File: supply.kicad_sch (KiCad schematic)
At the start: 1 part

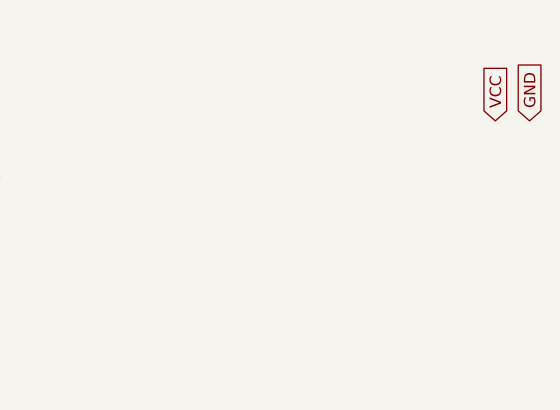
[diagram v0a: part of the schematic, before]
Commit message: now using correct VCC and GND symbols
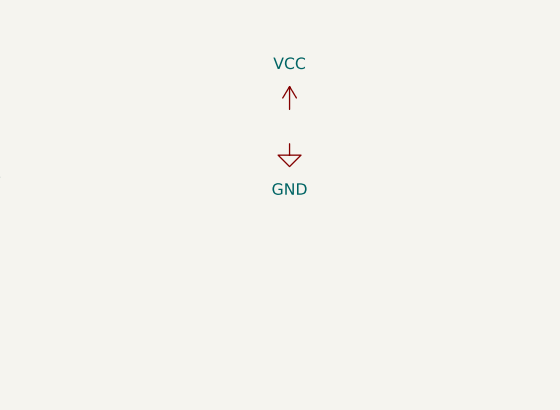
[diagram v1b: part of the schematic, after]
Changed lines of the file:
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@@
 (kicad_sch (version 20211123) (generator eeschema)
   (paper "A4")
-  (global_label "VCC" (shape input) (at 144.78 36.83 90) (fields_autoplaced)
-    (effects (font (size 1.27 1.27)) (justify left))
-    (property "Intersheet References" "${INTERSHEET_REFS}" (id 0) (at 144.7006 30.7883 90)
-      (effects (font (size 1.27 1.27)) (justify left) hide)
+  (symbol (lib_id "power:GND") (at 121.92 39.37 0) (unit 1)
+    (in_bom yes) (on_board yes) (fields_autoplaced)
+    (property "Reference" "#PWR?" (id 0) (at 121.92 45.72 0)
+      (effects (font (size 1.27 1.27)) hide)
     )
-  )
-  (global_label "GND" (shape input) (at 148.59 36.83 90) (fields_autoplaced)
-    (effects (font (size 1.27 1.27)) (justify left))
-    (property "Intersheet References" "${INTERSHEET_REFS}" (id 0) (at 148.5106 30.5464 90)
-      (effects (font (size 1.27 1.27)) (justify left) hide)
+    (property "Value" "GND" (id 1) (at 121.92 44.45 0))
+    (property "Footprint" "" (id 2) (at 121.92 39.37 0)
+      (effects (font (size 1.27 1.27)) hide)
     )
+    (property "Datasheet" "" (id 3) (at 121.92 39.37 0)
+      (effects (font (size 1.27 1.27)) hide)
+    )
+    (pin "1")
   )
   (symbol (lib_id "supply:ISL9307IRTAANFZ-T7A") (at 38.1 45.72 0) (unit 1)
@@
     (pin "9")
   )
+  (symbol (lib_id "power:VCC") (at 121.92 35.56 0) (unit 1)
+    (in_bom yes) (on_board yes) (fields_autoplaced)
+    (property "Reference" "#PWR?" (id 0) (at 121.92 39.37 0)
+      (effects (font (size 1.27 1.27)) hide)
+    )
+    (property "Value" "VCC" (id 1) (at 121.92 30.48 0))
+    (property "Footprint" "" (id 2) (at 121.92 35.56 0)
+      (effects (font (size 1.27 1.27)) hide)
+    )
+    (property "Datasheet" "" (id 3) (at 121.92 35.56 0)
+      (effects (font (size 1.27 1.27)) hide)
+    )
+    (pin "1")
+  )
 )

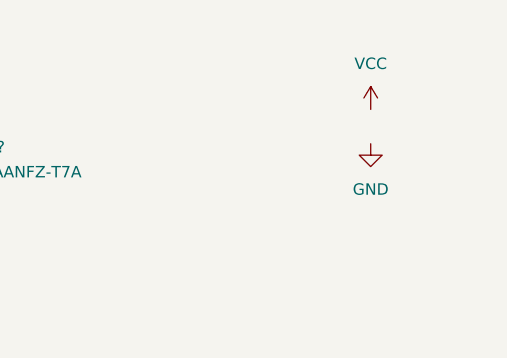
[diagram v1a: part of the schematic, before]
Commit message: added esp32 schematic && updated supply symbols
Signed-off-by: Tobias Gent <gent.tobias@gmail.com>
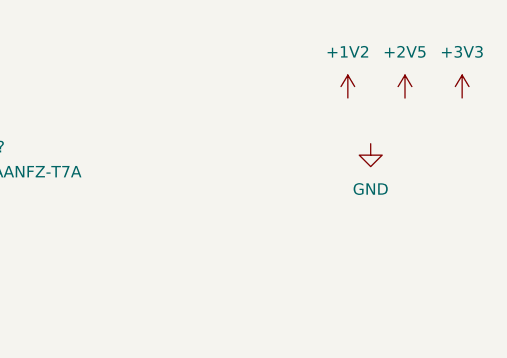
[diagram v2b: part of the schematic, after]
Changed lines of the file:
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@@
     (pin "9")
   )
-  (symbol (lib_id "power:VCC") (at 121.92 35.56 0) (unit 1)
+  (symbol (lib_id "power:+2V5") (at 125.73 34.29 0) (unit 1)
     (in_bom yes) (on_board yes) (fields_autoplaced)
-    (property "Reference" "#PWR?" (id 0) (at 121.92 39.37 0)
+    (property "Reference" "#PWR?" (id 0) (at 125.73 38.1 0)
       (effects (font (size 1.27 1.27)) hide)
     )
-    (property "Value" "VCC" (id 1) (at 121.92 30.48 0))
-    (property "Footprint" "" (id 2) (at 121.92 35.56 0)
+    (property "Value" "+2V5" (id 1) (at 125.73 29.21 0))
+    (property "Footprint" "" (id 2) (at 125.73 34.29 0)
       (effects (font (size 1.27 1.27)) hide)
     )
-    (property "Datasheet" "" (id 3) (at 121.92 35.56 0)
+    (property "Datasheet" "" (id 3) (at 125.73 34.29 0)
       (effects (font (size 1.27 1.27)) hide)
     )
+    (pin "1")
+  )
+  (symbol (lib_id "power:+1V2") (at 119.38 34.29 0) (unit 1)
+    (in_bom yes) (on_board yes) (fields_autoplaced)
+    (property "Reference" "#PWR?" (id 0) (at 119.38 38.1 0)
+      (effects (font (size 1.27 1.27)) hide)
+    )
+    (property "Value" "+1V2" (id 1) (at 119.38 29.21 0))
+    (property "Footprint" "" (id 2) (at 119.38 34.29 0)
+      (effects (font (size 1.27 1.27)) hide)
+    )
+    (property "Datasheet" "" (id 3) (at 119.38 34.29 0)
+      (effects (font (size 1.27 1.27)) hide)
+    )
+    (pin "1")
+  )
+  (symbol (lib_id "power:+3V3") (at 132.08 34.29 0) (unit 1)
+    (in_bom yes) (on_board yes) (fields_autoplaced)
+    (property "Reference" "#PWR?" (id 0) (at 132.08 38.1 0)
+      (effects (font (size 1.27 1.27)) hide)
+    )
+    (property "Value" "+3V3" (id 1) (at 132.08 29.21 0))
+    (property "Footprint" "" (id 2) (at 132.08 34.29 0)
+      (effects (font (size 1.27 1.27)) hide)
+    )
+    (property "Datasheet" "" (id 3) (at 132.08 34.29 0)
+      (effects (font (size 1.27 1.27)) hide)
+    )

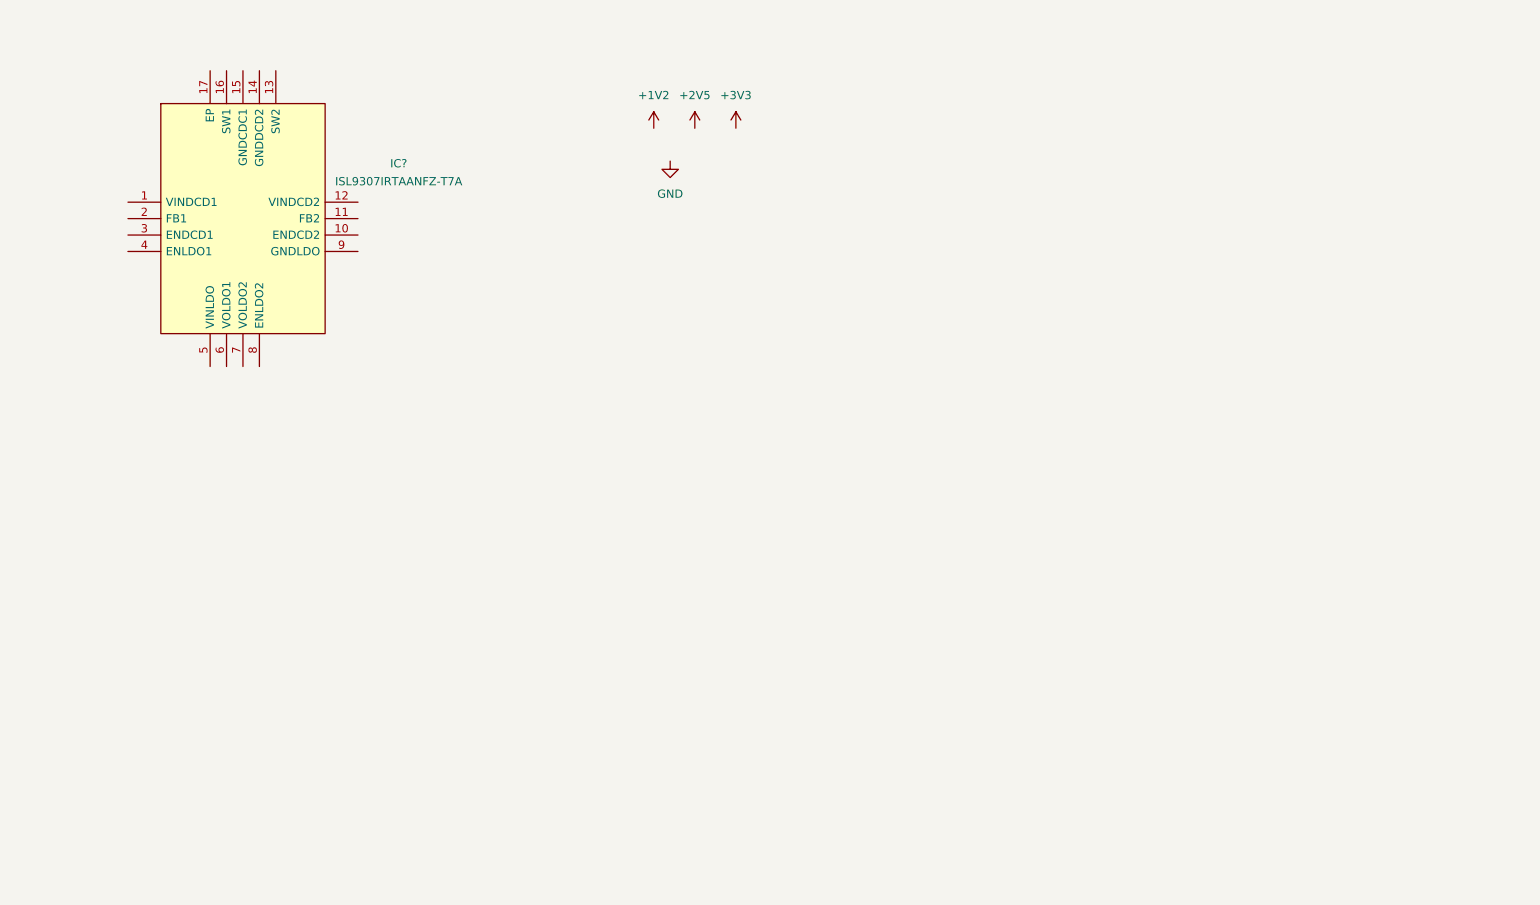
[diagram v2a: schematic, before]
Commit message: Added Supply
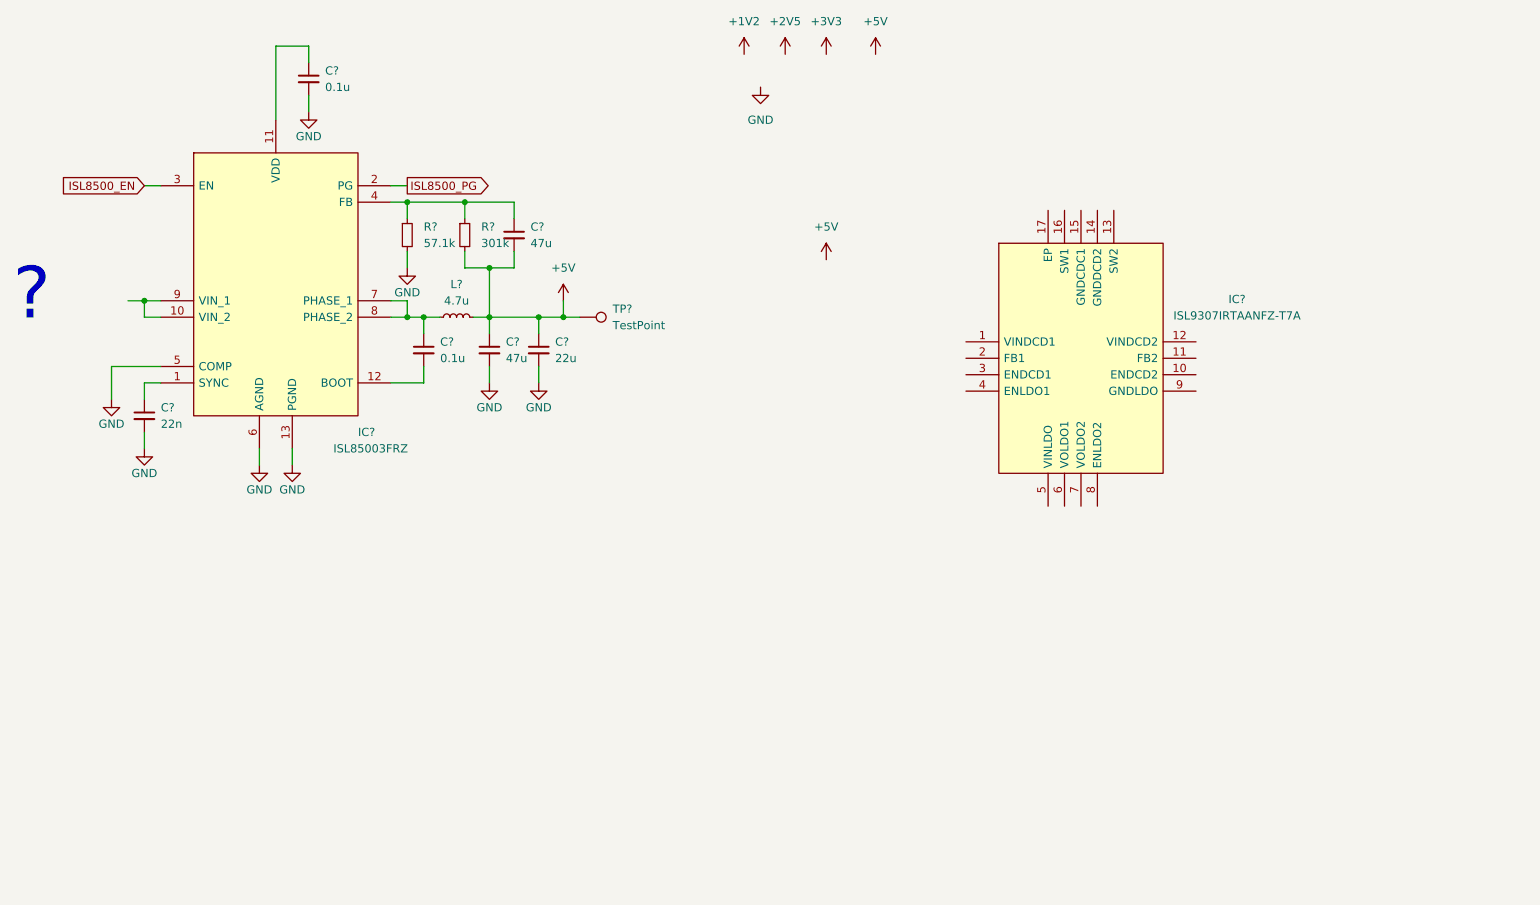
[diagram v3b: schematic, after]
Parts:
- added C?: 22u, symbol Device:C_Small
- added C? (x2): 47u, symbol Device:C_Small
- added C? (x2): 0.1u, symbol Device:C_Small
- added C?: 22n, symbol Device:C_Small
- added IC?: ISL85003FRZ, SON50P300X400X90-13N, symbol supply:ISL85003FRZ
- added L?: 4.7u, symbol Device:L_Small
- added R?: 301k, symbol Device:R_Small
- added R?: 57.1k, symbol Device:R_Small
- added TP?: TestPoint, symbol Connector:TestPoint
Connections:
- net GND: now also C?.2, C?.2, C?.2, C?.2, IC?.13 (PGND), IC?.5 (COMP), IC?.6 (AGND), R?.2
- new net: C?.1, IC?.4 (FB), R?.1, R?.1
- new net: C?.1, IC?.1 (SYNC)
- new net: IC?.10 (VIN_2), IC?.9 (VIN_1)
- new net: C?.1, IC?.11 (VDD)
- new net: C?.2, IC?.12 (BOOT)
- new net: C?.1, IC?.7 (PHASE_1), IC?.8 (PHASE_2), L?.1
- new net +5V: C?.1, C?.1, C?.2, L?.2, R?.2, TP?.1
- new net ISL8500_EN: IC?.3 (EN)
- new net ISL8500_PG: IC?.2 (PG)
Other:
- note added: "?"
- moved on the sheet: IC?

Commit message: modified supply symbols + added layout
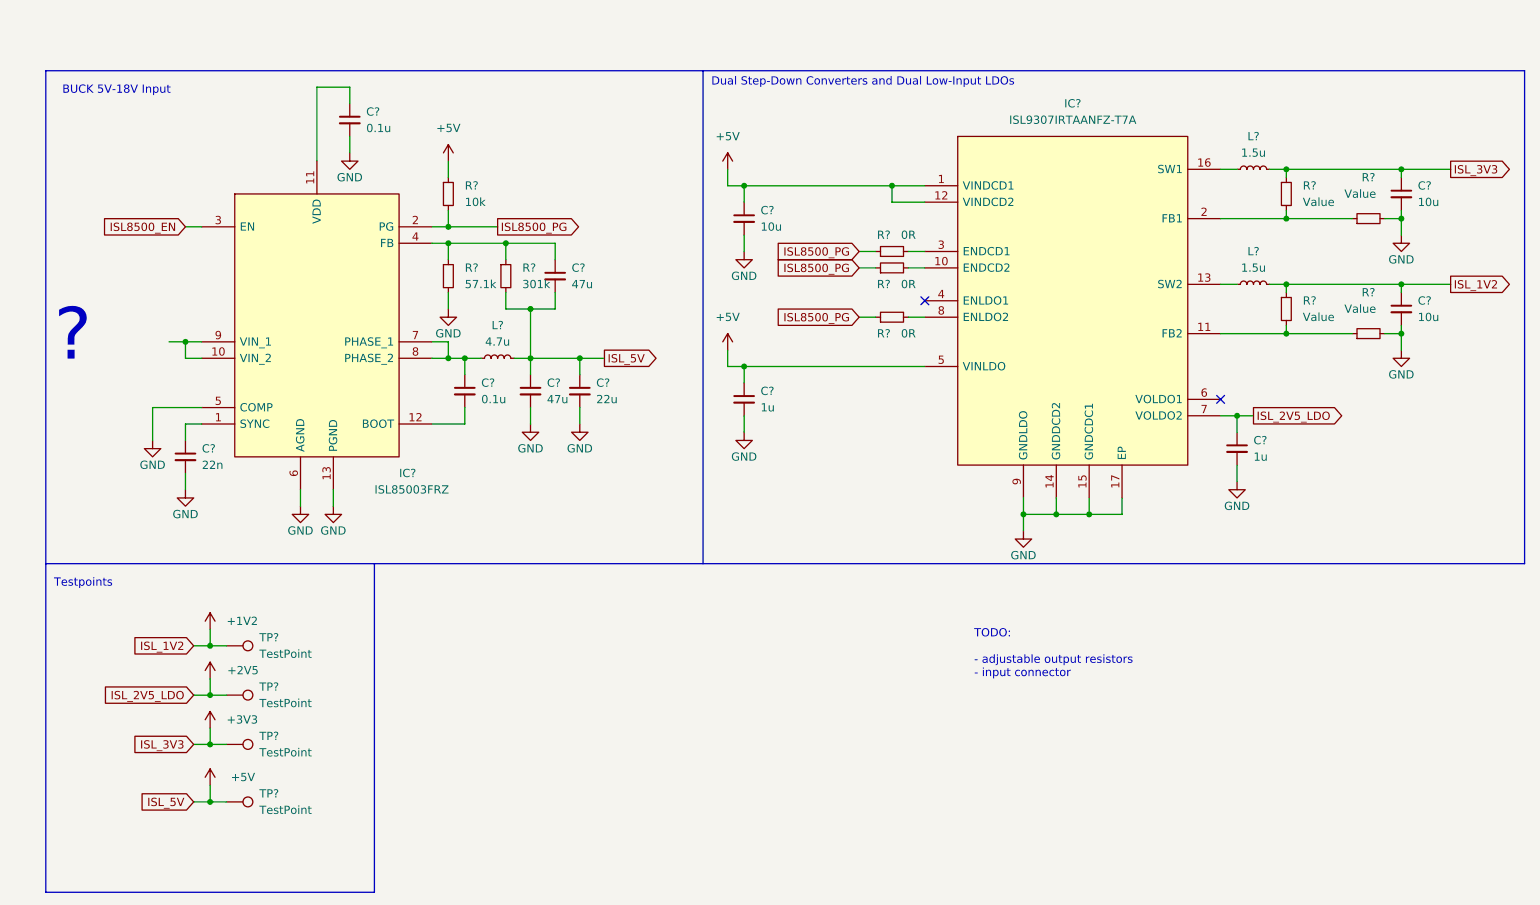
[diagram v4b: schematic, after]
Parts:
- removed TP?: TestPoint, symbol Connector:TestPoint
- added C? (x3): 10u, symbol Device:C_Small
- added C? (x2): 1u, symbol Device:C_Small
- added L? (x2): 1.5u, symbol Device:L_Small
- added R? (x4): Value, symbol Device:R_Small
- added R? (x3): 0R, symbol Device:R_Small
- added R?: 10k, symbol Device:R_Small
- added TP? (x4): TestPoint, symbol Connector:TestPoint
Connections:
- net +1V2: now also C?.1, L?.2, R?.1, TP?.1
- net +2V5: now also IC?.7 (VOLDO2), C?.1, TP?.1
- net +3V3: now also C?.1, L?.2, R?.1, TP?.1
- net +5V: now also IC?.1 (VINDCD1), IC?.12 (VINDCD2), IC?.5 (VINLDO), C?.1, C?.1, R?.1, TP?.1
- net GND: now also IC?.14 (GNDDCD2), IC?.15 (GNDCDC1), IC?.17 (EP), IC?.9 (GNDLDO), C?.2, C?.2, C?.2, C?.2, C?.2, R?.2, R?.2
- net ISL8500_PG: now also R?.1, R?.1, R?.1, R?.2
- net at IC?.10 (ENDCD2): now also R?.2
- net at IC?.11 (FB2): now also R?.1, R?.2
- net at IC?.13 (SW2): now also L?.1
- net at IC?.16 (SW1): now also L?.1
- net at IC?.2 (FB1): now also R?.1, R?.2
- net at IC?.3 (ENDCD1): now also R?.2
- net at IC?.8 (ENLDO2): now also R?.2
- no-connect marks 0 -> 2
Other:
- note added: "BUCK 5V-18V Input"
- note added: "Dual Step-Down Converters and Dual Low-Input LDOs"
- note added: "TODO: - adjustable output resistors - input connector"
- note added: "Testpoints"
- moved on the sheet: C?, IC?, L?, R?

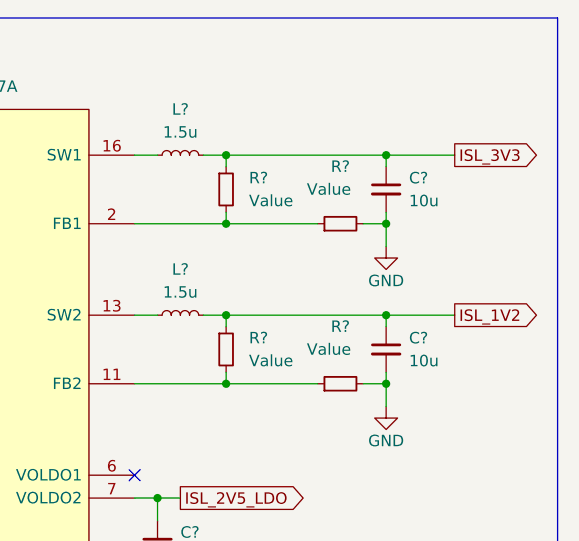
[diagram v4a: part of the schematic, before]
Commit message: supply: changed voltage divider values on ISL9307
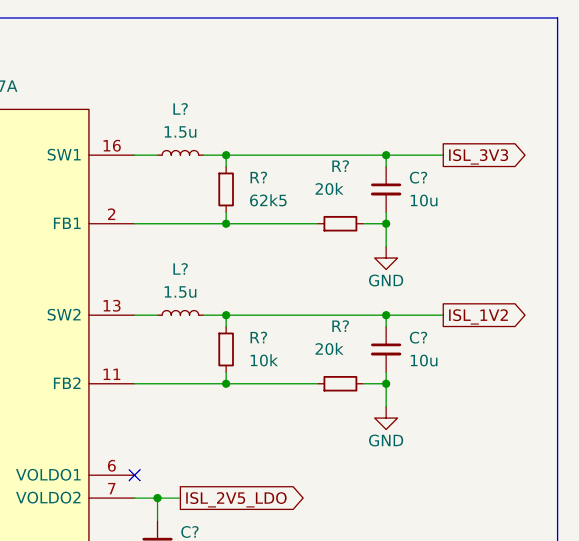
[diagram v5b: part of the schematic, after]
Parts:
- R?: value Value -> 62k5
- R?: value Value -> 10k
- R? (x2): value Value -> 20k
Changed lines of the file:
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@@
     (stroke (width 0) (type default) (color 0 0 0 0))
   )
-  (wire (pts (xy 234.95 58.42) (xy 242.57 58.42))
+  (wire (pts (xy 234.95 58.42) (xy 241.3 58.42))
     (stroke (width 0) (type default) (color 0 0 0 0))
   )
@@
     (stroke (width 0) (type default) (color 0 0 0 0))
   )
-  (wire (pts (xy 234.95 40.64) (xy 242.57 40.64))
+  (wire (pts (xy 234.95 40.64) (xy 241.3 40.64))
     (stroke (width 0) (type default) (color 0 0 0 0))
   )
@@
     )
   )
-  (global_label "ISL_1V2" (shape output) (at 242.57 58.42 0) (fields_autoplaced)
+  (global_label "ISL_1V2" (shape output) (at 241.3 58.42 0) (fields_autoplaced)
     (effects (font (size 1.27 1.27)) (justify left))
-    (property "Intersheet References" "${INTERSHEET_REFS}" (id 0) (at 252.3007 58.3406 0)
+    (property "Intersheet References" "${INTERSHEET_REFS}" (id 0) (at 251.0307 58.3406 0)
       (effects (font (size 1.27 1.27)) (justify left) hide)
     )
@@
     )
   )
-  (global_label "ISL_3V3" (shape output) (at 242.57 40.64 0) (fields_autoplaced)
+  (global_label "ISL_3V3" (shape output) (at 241.3 40.64 0) (fields_autoplaced)
     (effects (font (size 1.27 1.27)) (justify left))
-    (property "Intersheet References" "${INTERSHEET_REFS}" (id 0) (at 252.3007 40.5606 0)
+    (property "Intersheet References" "${INTERSHEET_REFS}" (id 0) (at 251.0307 40.5606 0)
       (effects (font (size 1.27 1.27)) (justify left) hide)
     )
@@
       (effects (font (size 1.27 1.27)) (justify left))
     )
-    (property "Value" "Value" (id 1) (at 219.71 45.7199 0)
+    (property "Value" "62k5" (id 1) (at 219.71 45.7199 0)
       (effects (font (size 1.27 1.27)) (justify left))
     )
@@
       (effects (font (size 1.27 1.27)) (justify left))
     )
-    (property "Value" "Value" (id 1) (at 219.71 63.4999 0)
+    (property "Value" "10k" (id 1) (at 219.71 63.4999 0)
       (effects (font (size 1.27 1.27)) (justify left))
     )
@@
     (in_bom yes) (on_board yes)
     (property "Reference" "R?" (id 0) (at 229.87 41.91 90))
-    (property "Value" "Value" (id 1) (at 228.6 44.45 90))
+    (property "Value" "20k" (id 1) (at 228.6 44.45 90))
     (property "Footprint" "" (id 2) (at 229.87 48.26 0)
       (effects (font (size 1.27 1.27)) hide)
@@
     (in_bom yes) (on_board yes)
     (property "Reference" "R?" (id 0) (at 229.87 59.69 90))
-    (property "Value" "Value" (id 1) (at 228.6 62.23 90))
+    (property "Value" "20k" (id 1) (at 228.6 62.23 90))
     (property "Footprint" "" (id 2) (at 229.87 66.04 0)
       (effects (font (size 1.27 1.27)) hide)

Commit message: supply: added formula for buck voltage dividers
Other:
- note added: "R1 = R2 *( (Vout / 0.8V) - 1)"
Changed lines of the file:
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@@
+    (effects (font (size 1.27 1.27)) (justify left bottom))
+  )
+  (text "R1 = R2 *( (Vout / 0.8V) - 1)" (at 217.17 31.75 0)
     (effects (font (size 1.27 1.27)) (justify left bottom))
   )

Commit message: supply: added barrel jack
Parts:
- added J?: Barrel_Jack, symbol Connector:Barrel_Jack
- added J?: Conn_01x02_Male, symbol Connector:Conn_01x02_Male
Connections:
- net GND: now also J?.2, J?.2 (Pin_2)
- net at IC?.10 (VIN_2), IC?.9 (VIN_1): now also J?.1, J?.1 (Pin_1)
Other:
- note removed: "?"
- moved on the sheet: C?, IC?, L?, R?
